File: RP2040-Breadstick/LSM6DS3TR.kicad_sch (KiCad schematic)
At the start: 2 parts, among them U401 6-Axis IMU

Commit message: things mike needs to fix
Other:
- note removed: "Add more capacitance, IMUs are sensitive."
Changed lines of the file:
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@@
-    (effects (font (size 1.27 1.27)) (justify left bottom))
-  )
-  (text "Add more capacitance,\nIMUs are sensitive." (at 162.56 102.87 0)
     (effects (font (size 1.27 1.27)) (justify left bottom))
   )

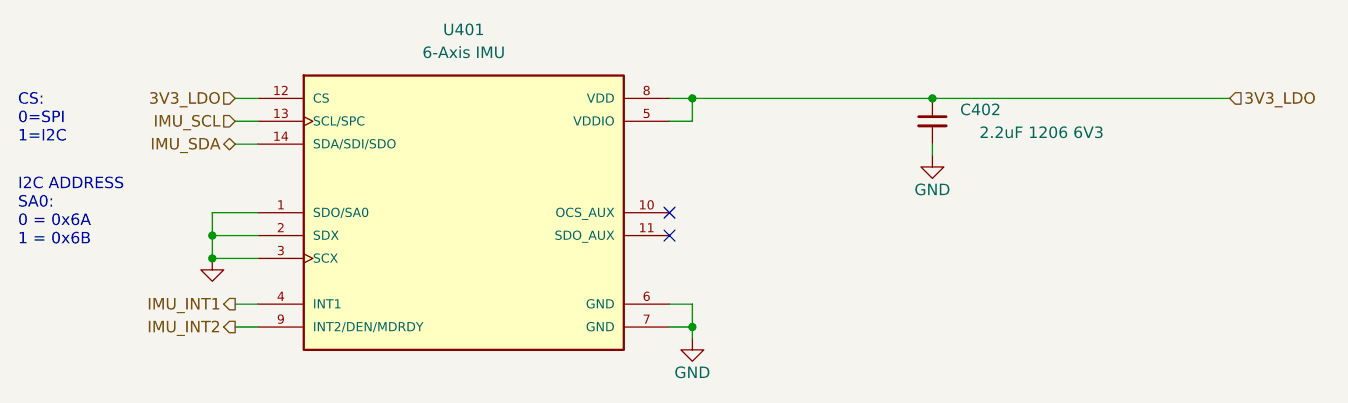
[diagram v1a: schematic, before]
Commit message: Fixed BOM issues, adjusted wires, updated silkscreen
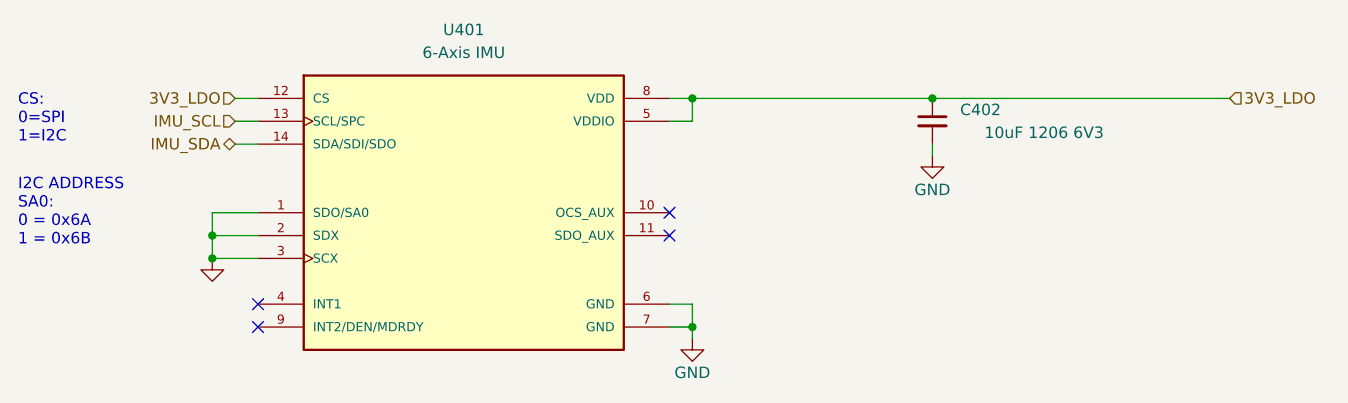
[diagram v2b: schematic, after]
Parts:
- C402: value 2.2uF 1206 6V3 -> 10uF 1206 6V3; Digikey 1276-1134-6-ND -> 1276-3107-1-ND; Manufacturer_Part_Number CL10B225KP8NNNC -> CL31B106KQHNFNE; Mouser 187-CL10B225KP8NNNC -> 187-CL31B106KQHNFNE
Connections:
- net IMU_INT1: no longer names the net of U401.4 (INT1)
- net IMU_INT2: no longer names the net of U401.9 (INT2/DEN/MDRDY)
- no-connect marks 2 -> 4
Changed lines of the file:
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@@
   (junction (at 95.25 101.6) (diameter 0) (color 0 0 0 0)
   )
+  (no_connect (at 100.33 109.22))
   (no_connect (at 146.05 101.6))
   (no_connect (at 146.05 99.06))
+  (no_connect (at 100.33 111.76))
   (wire (pts (xy 146.05 88.9) (xy 148.59 88.9))
     (stroke (width 0) (type default))
@@
   )
   (wire (pts (xy 95.25 99.06) (xy 95.25 101.6))
-    (stroke (width 0) (type default))
-  )
-  (wire (pts (xy 97.79 109.22) (xy 100.33 109.22))
     (stroke (width 0) (type default))
   )
@@
   )
   (wire (pts (xy 148.59 86.36) (xy 175.26 86.36))
-    (stroke (width 0) (type default))
-  )
-  (wire (pts (xy 97.79 111.76) (xy 100.33 111.76))
     (stroke (width 0) (type default))
   )
@@
     (effects (font (size 1.27 1.27)) (justify left))
   )
-  (hierarchical_label "IMU_INT2" (shape output) (at 97.79 111.76 180) (fields_autoplaced)
-    (effects (font (size 1.27 1.27)) (justify right))
-  )
   (hierarchical_label "3V3_LDO" (shape input) (at 97.79 86.36 180) (fields_autoplaced)
     (effects (font (size 1.27 1.27)) (justify right))
   )
   (hierarchical_label "IMU_SDA" (shape bidirectional) (at 97.79 91.44 180) (fields_autoplaced)
-    (effects (font (size 1.27 1.27)) (justify right))
-  )
-  (hierarchical_label "IMU_INT1" (shape output) (at 97.79 109.22 180) (fields_autoplaced)
     (effects (font (size 1.27 1.27)) (justify right))
   )
@@
       (effects (font (size 1.27 1.27)) (justify left))
     )
-    (property "Value" "2.2uF 1206 6V3" (at 194.31 90.17 0)
+    (property "Value" "10uF 1206 6V3" (at 194.31 90.17 0)
       (effects (font (size 1.27 1.27)) (justify left))
     )
@@
       (effects (font (size 1.27 1.27)) hide)
     )
-    (property "Digikey" "1276-1134-6-ND" (at 175.26 88.9 0)
+    (property "Digikey" "1276-3107-1-ND" (at 175.26 88.9 0)
       (effects (font (size 1.27 1.27)) hide)
     )
@@
       (effects (font (size 1.27 1.27)) hide)
     )
-    (property "Manufacturer_Part_Number" "CL10B225KP8NNNC" (at 175.26 88.9 0)
+    (property "Manufacturer_Part_Number" "CL31B106KQHNFNE" (at 175.26 88.9 0)
       (effects (font (size 1.27 1.27)) hide)
     )
-    (property "Mouser" "187-CL10B225KP8NNNC" (at 175.26 88.9 0)
+    (property "Mouser" "187-CL31B106KQHNFNE" (at 175.26 88.9 0)
       (effects (font (size 1.27 1.27)) hide)
     )

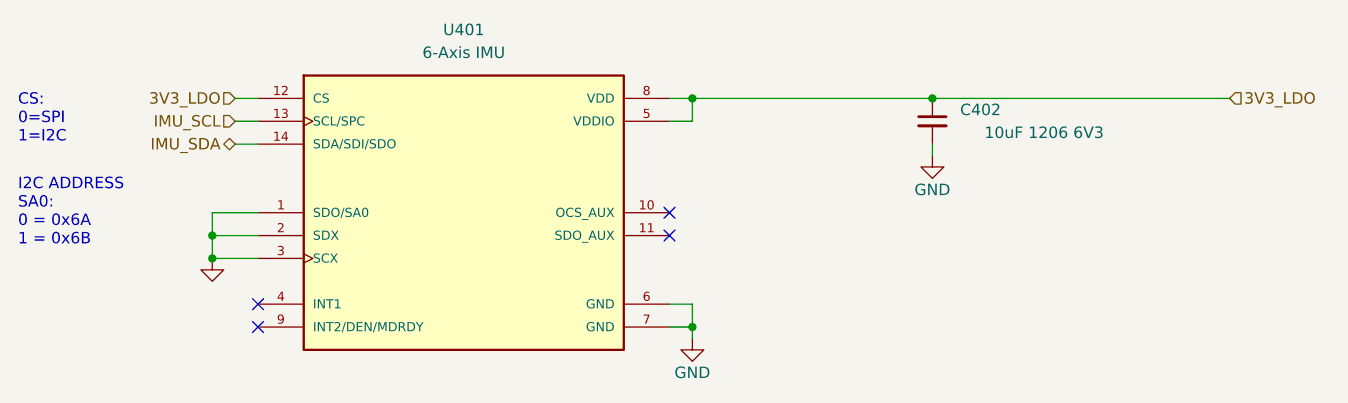
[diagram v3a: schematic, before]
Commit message: Cleaned up schematic, added renders, made images for documentation
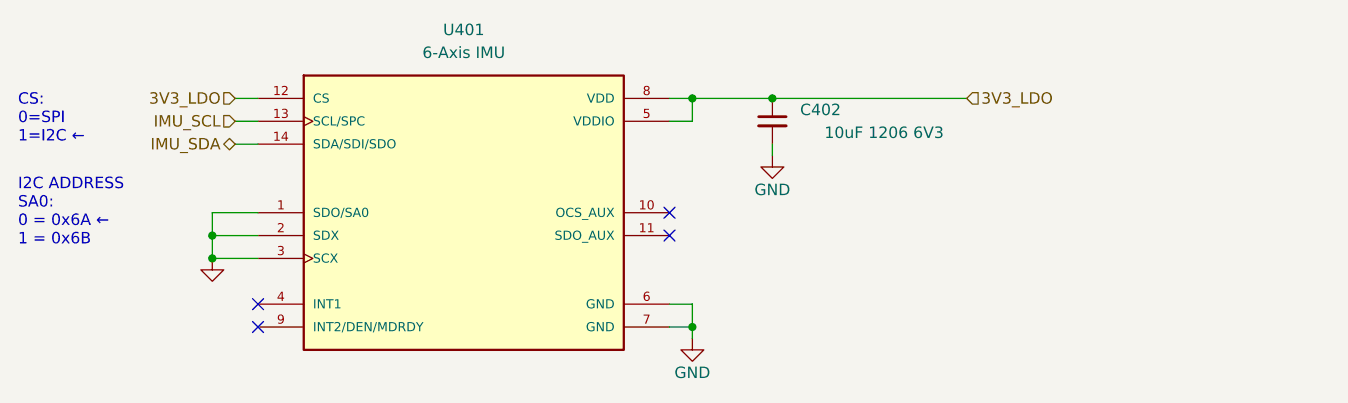
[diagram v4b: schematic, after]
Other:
- note added: "CS: 0=SPI 1=I2C ←"
- note added: "I2C ADDRESS SA0: 0 = 0x6A ← 1 = 0x6B"
- note removed: "CS: 0=SPI 1=I2C"
- note removed: "I2C ADDRESS SA0: 0 = 0x6A 1 = 0x6B"
- moved on the sheet: C402
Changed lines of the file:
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@@
   (title_block
     (title "Raspberry Breadstick")
-    (date "2023-07-02")
+    (date "2023-11-04")
     (rev "0.2")
     (company "J & R Creative Technologies Inc.")
@@
     (comment 5 "https://shop.breadstick.ca/")
   )
-  (junction (at 175.26 86.36) (diameter 0) (color 0 0 0 0)
-  )
   (junction (at 148.59 111.76) (diameter 0) (color 0 0 0 0)
   )
   (junction (at 148.59 86.36) (diameter 0) (color 0 0 0 0)
+  )
+  (junction (at 157.48 86.36) (diameter 0) (color 0 0 0 0)
   )
   (junction (at 95.25 104.14) (diameter 0) (color 0 0 0 0)
@@
   (no_connect (at 146.05 99.06))
   (no_connect (at 100.33 111.76))
+  (wire (pts (xy 157.48 86.36) (xy 179.07 86.36))
+    (stroke (width 0) (type default))
+  )
   (wire (pts (xy 146.05 88.9) (xy 148.59 88.9))
     (stroke (width 0) (type default))
@@
     (stroke (width 0) (type default))
   )
-  (wire (pts (xy 148.59 86.36) (xy 175.26 86.36))
+  (wire (pts (xy 148.59 86.36) (xy 157.48 86.36))
     (stroke (width 0) (type default))
   )
-  (wire (pts (xy 175.26 91.44) (xy 175.26 92.71))
+  (wire (pts (xy 157.48 91.44) (xy 157.48 92.71))
     (stroke (width 0) (type default))
   )
   (wire (pts (xy 146.05 86.36) (xy 148.59 86.36))
-    (stroke (width 0) (type default))
-  )
-  (wire (pts (xy 175.26 86.36) (xy 208.28 86.36))
     (stroke (width 0) (type default))
   )
@@
     (stroke (width 0) (type default))
   )
-  (text "I2C ADDRESS\nSA0:\n0 = 0x6A\n1 = 0x6B" (at 73.66 102.87 0)
+  (text "I2C ADDRESS\nSA0:\n0 = 0x6A ←\n1 = 0x6B" (at 73.66 102.87 0)
     (effects (font (size 1.27 1.27)) (justify left bottom))
   )
-  (text "CS:\n0=SPI\n1=I2C" (at 73.66 91.44 0)
+  (text "CS:\n0=SPI\n1=I2C ←" (at 73.66 91.44 0)
     (effects (font (size 1.27 1.27)) (justify left bottom))
   )
@@
     (effects (font (size 1.27 1.27)) (justify right))
   )
-  (hierarchical_label "3V3_LDO" (shape input) (at 208.28 86.36 0) (fields_autoplaced)
+  (hierarchical_label "3V3_LDO" (shape input) (at 179.07 86.36 0) (fields_autoplaced)
     (effects (font (size 1.27 1.27)) (justify left))
   )
@@
     (effects (font (size 1.27 1.27)) (justify right))
   )
-  (symbol (lib_id "Device:C_Small") (at 175.26 88.9 0) (mirror y) (unit 1)
+  (symbol (lib_id "Device:C_Small") (at 157.48 88.9 0) (mirror y) (unit 1)
     (in_bom yes) (on_board yes) (dnp no)
-    (property "Reference" "C402" (at 182.88 87.63 0)
+    (property "Reference" "C402" (at 165.1 87.63 0)
       (effects (font (size 1.27 1.27)) (justify left))
     )
-    (property "Value" "10uF 1206 6V3" (at 194.31 90.17 0)
+    (property "Value" "10uF 1206 6V3" (at 176.53 90.17 0)
       (effects (font (size 1.27 1.27)) (justify left))
     )
-    (property "Footprint" "Capacitor_SMD:C_1206_3216Metric" (at 175.26 88.9 0)
+    (property "Footprint" "Capacitor_SMD:C_1206_3216Metric" (at 157.48 88.9 0)
       (effects (font (size 1.27 1.27)) hide)
     )
-    (property "Datasheet" "~" (at 175.26 88.9 0)
+    (property "Datasheet" "~" (at 157.48 88.9 0)
       (effects (font (size 1.27 1.27)) hide)
     )
-    (property "JLCPCB P/N" "" (at 175.26 88.9 0)
+    (property "JLCPCB P/N" "" (at 157.48 88.9 0)
       (effects (font (size 1.27 1.27)) hide)
     )
-    (property "Digikey" "1276-3107-1-ND" (at 175.26 88.9 0)
+    (property "Digikey" "1276-3107-1-ND" (at 157.48 88.9 0)
       (effects (font (size 1.27 1.27)) hide)
     )
-    (property "Manufacturer" "Samsung Electro-Mechanics" (at 175.26 88.9 0)
+    (property "Manufacturer" "Samsung Electro-Mechanics" (at 157.48 88.9 0)
       (effects (font (size 1.27 1.27)) hide)
     )
-    (property "Manufacturer_Part_Number" "CL31B106KQHNFNE" (at 175.26 88.9 0)
+    (property "Manufacturer_Part_Number" "CL31B106KQHNFNE" (at 157.48 88.9 0)
       (effects (font (size 1.27 1.27)) hide)
     )
-    (property "Mouser" "187-CL31B106KQHNFNE" (at 175.26 88.9 0)
+    (property "Mouser" "187-CL31B106KQHNFNE" (at 157.48 88.9 0)
       (effects (font (size 1.27 1.27)) hide)
     )
-    (property "Package" "1206" (at 175.26 88.9 0)
+    (property "Package" "1206" (at 157.48 88.9 0)
       (effects (font (size 1.27 1.27)) hide)
     )
-    (property "LCSC" "" (at 175.26 88.9 0)
+    (property "LCSC" "" (at 157.48 88.9 0)
       (effects (font (size 1.27 1.27)) hide)
     )
@@
     )
   )
-  (symbol (lib_id "power:GND") (at 175.26 92.71 0) (mirror y) (unit 1)
+  (symbol (lib_id "power:GND") (at 157.48 92.71 0) (mirror y) (unit 1)
     (in_bom yes) (on_board yes) (dnp no)
-    (property "Reference" "#PWR0404" (at 175.26 99.06 0)
+    (property "Reference" "#PWR0404" (at 157.48 99.06 0)
       (effects (font (size 1.27 1.27)) hide)
     )
-    (property "Value" "GND" (at 175.26 96.52 0)
+    (property "Value" "GND" (at 157.48 96.52 0)
       (effects (font (size 1.27 1.27)))
     )
-    (property "Footprint" "" (at 175.26 92.71 0)
+    (property "Footprint" "" (at 157.48 92.71 0)
       (effects (font (size 1.27 1.27)) hide)
     )
-    (property "Datasheet" "" (at 175.26 92.71 0)
+    (property "Datasheet" "" (at 157.48 92.71 0)
       (effects (font (size 1.27 1.27)) hide)
     )

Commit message: Fixed pinout labels
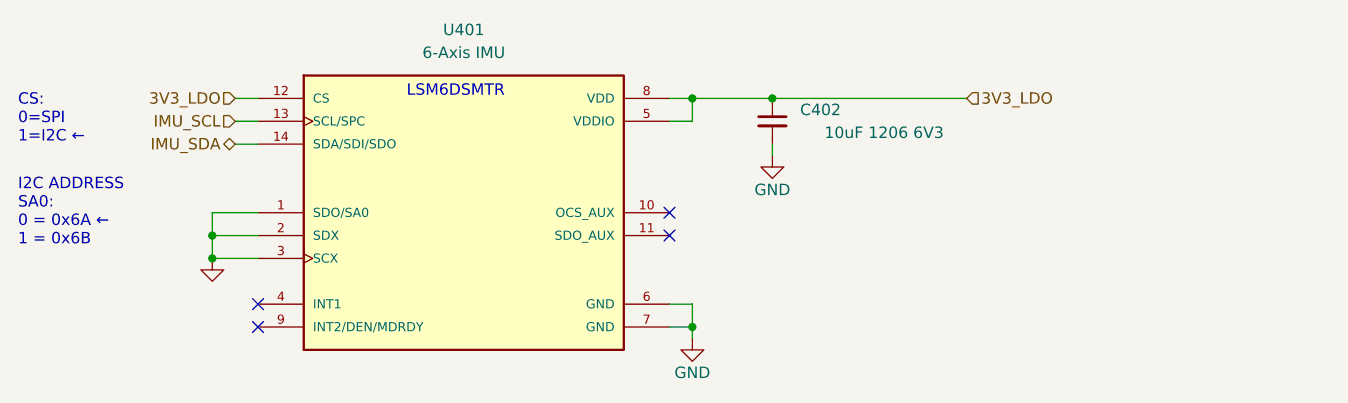
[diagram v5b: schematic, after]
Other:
- note added: "LSM6DSMTR"
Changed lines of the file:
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@@
+    (effects (font (size 1.27 1.27)) (justify left bottom))
+  )
+  (text "LSM6DSMTR" (at 116.84 86.36 0)
     (effects (font (size 1.27 1.27)) (justify left bottom))
   )
